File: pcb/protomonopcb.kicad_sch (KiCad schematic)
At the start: 149 parts

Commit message: Just another periodic push
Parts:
- removed LED1, LED10, LED11, LED12, LED13, LED14, LED15, LED16, LED17, LED18, LED19, LED2, LED20, LED21, LED22, LED23, LED24, LED26, LED27, LED28, LED29, LED3, LED30, LED31, LED32, LED33, LED34, LED35, LED37, LED38, LED39, LED4, LED40, LED41, LED42, LED43, LED44, LED45, LED46, LED47, LED48, LED49, LED5, LED50, LED6, LED7, LED8, LED9: SK6812MINI-E, LED_SMD:LED_SK6812MINI_PLCC4_3.5x3.5mm_P1.75mm, symbol PCM_marbastlib-various:SK6812MINI-E
- added D25, D36, D51, D52: LED, LED_THT:LED_D3.0mm, symbol Device:LED
- added R5, R6, R7, R8: 1k, Resistor_THT:R_Axial_DIN0204_L3.6mm_D1.6mm_P7.62mm_Horizontal, symbol Device:R
- A1: footprint Module:RaspberryPi_Pico_Common_Unspecified -> pico_without_keepout_area:RaspberryPi_Pico_Common_Unspecified
- CH1, CH10, CH11, CH12, CH13, CH14, CH15, CH16, CH17, CH18, CH19, CH2, CH20, CH21, CH22, CH23, CH24, CH26, CH27, CH28, CH29, CH3, CH30, CH31, CH32, CH33, CH34, CH35, CH37, CH38, CH39, CH4, CH40, CH41, CH42, CH43, CH44, CH45, CH46, CH47, CH48, CH49, CH5, CH50, CH6, CH7, CH8, CH9: footprint PCM_marbastlib-xp-gateron_lp:SW_KS33_HS_KS-2P02B01-02_HS_1u -> packed_switches_library:SW_KS33_HS_1u_18.5mm
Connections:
- net GND: now also D25.1 (K), D36.1 (K), D51.1 (K), D52.1 (K)
- net c0: now also A1.12 (GPIO9); no longer A1.14 (GPIO10), CH47.1, CH49.1
- net c1: now also A1.14 (GPIO10), CH49.1; no longer A1.15 (GPIO11), CH37.1
- net c10: now also A1.27 (GPIO21), CH50.1; no longer A1.26 (GPIO20), CH44.1
- net c11: now also A1.29 (GPIO22); no longer A1.27 (GPIO21), CH48.1, CH50.1
- net c2: now also A1.15 (GPIO11), CH37.1; no longer A1.16 (GPIO12), CH38.1
- net c3: now also A1.16 (GPIO12); no longer A1.17 (GPIO13), CH39.1
- net c4: now also A1.17 (GPIO13), CH30.1, CH38.1; no longer A1.19 (GPIO14), CH29.1, CH40.1
- net c5: now also A1.19 (GPIO14), CH29.1, CH39.1; no longer A1.20 (GPIO15), CH30.1, CH41.1
- net c6: now also A1.22 (GPIO17); no longer A1.21 (GPIO16)
- net c7: now also A1.24 (GPIO18), CH47.1; no longer A1.22 (GPIO17), CH45.1
- net c8: now also A1.25 (GPIO19); no longer A1.24 (GPIO18), CH42.1
- net c9: now also A1.26 (GPIO20), CH44.1; no longer A1.25 (GPIO19), CH43.1
- net r0: now also D1.2 (A), D10.2 (A), D12.2 (A), D3.2 (A), D4.2 (A), D49.2 (A), D5.2 (A), D50.2 (A), D6.2 (A), D7.2 (A), D8.2 (A), D9.2 (A); no longer D37.2 (A), D38.2 (A), D39.2 (A), D40.2 (A), D41.2 (A), D42.2 (A), D43.2 (A), D44.2 (A), D45.2 (A), D46.2 (A), D47.2 (A), D48.2 (A)
- net r1: now also D11.2 (A), D15.2 (A), D16.2 (A), D17.2 (A), D18.2 (A), D19.2 (A), D2.2 (A), D20.2 (A), D21.2 (A), D22.2 (A), D42.2 (A), D48.2 (A); no longer D26.2 (A), D27.2 (A), D28.2 (A), D29.2 (A), D30.2 (A), D31.2 (A), D32.2 (A), D33.2 (A), D34.2 (A), D35.2 (A)
- net r2: now also D27.2 (A), D28.2 (A), D29.2 (A), D30.2 (A), D31.2 (A), D32.2 (A), D33.2 (A), D34.2 (A), D41.2 (A), D43.2 (A); no longer D1.2 (A), D12.2 (A), D15.2 (A), D16.2 (A), D17.2 (A), D18.2 (A), D19.2 (A), D20.2 (A), D21.2 (A), D22.2 (A)
- net r3: now also D26.2 (A), D35.2 (A), D37.2 (A), D38.2 (A), D39.2 (A), D40.2 (A), D44.2 (A), D45.2 (A), D46.2 (A), D47.2 (A); no longer D10.2 (A), D11.2 (A), D2.2 (A), D3.2 (A), D4.2 (A), D49.2 (A), D5.2 (A), D50.2 (A), D6.2 (A), D7.2 (A), D8.2 (A), D9.2 (A)
- net at R1.1: now also A1.7 (GPIO5); no longer A1.9 (GPIO6)
- net at R2.1: now also A1.9 (GPIO6); no longer A1.10 (GPIO7)
- net at R3.1: now also A1.10 (GPIO7); no longer A1.11 (GPIO8)
- net at R4.1: now also A1.11 (GPIO8); no longer A1.12 (GPIO9)
- net LED_1: now reaches A1.2 (GPIO1)
- net LED_1: now also R6.1
- net LED_2: now reaches A1.4 (GPIO2)
- net LED_2: now also R7.1
- net LED_3: now reaches A1.5 (GPIO3)
- net LED_3: now also R8.1
- net LED_in renamed LED_0
- net LED_0: now also R5.1
- new net: D52.2 (A), R8.2
- new net: D51.2 (A), R7.2
- new net: D25.2 (A), R5.2
- new net: D36.2 (A), R6.2
- new net ci: A1.20 (GPIO15), CH40.1, CH41.1, CH42.1
- new net cii: A1.21 (GPIO16), CH43.1, CH45.1, CH48.1
- no-connect marks 16 -> 10
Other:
- moved on the sheet: A1, CH1, CH10, CH11, CH12, CH13, CH14, CH15, CH16, CH17, CH18, CH19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

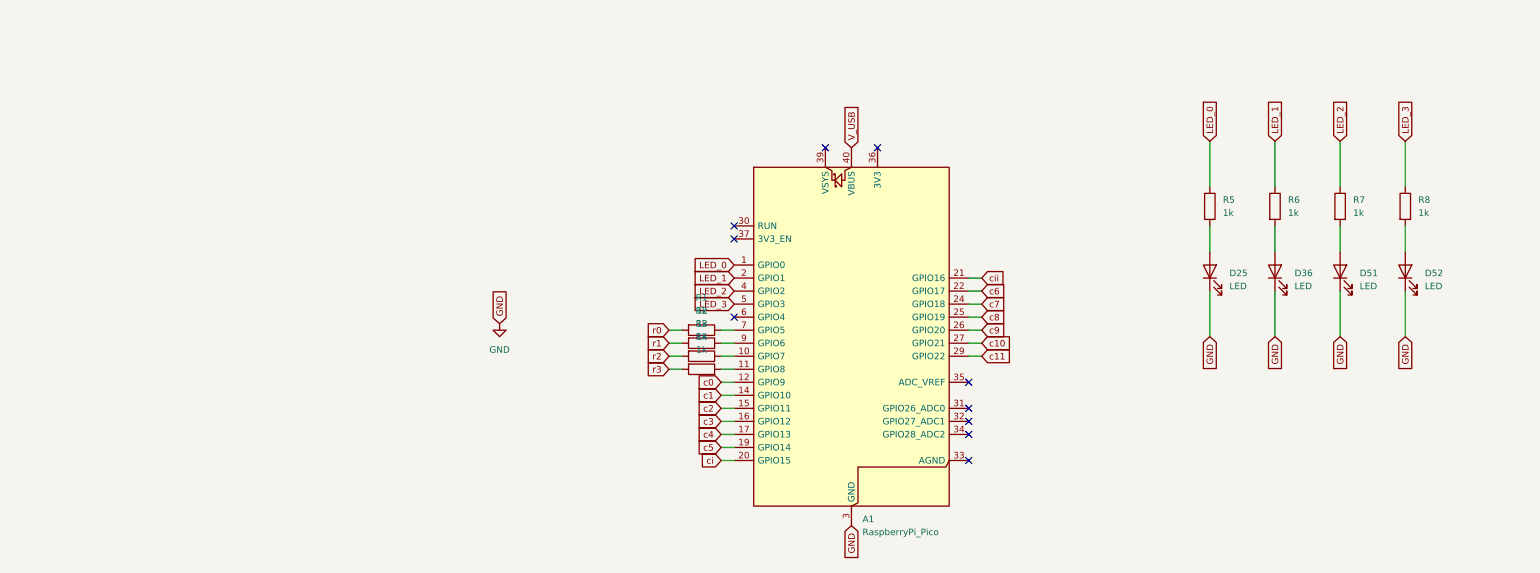
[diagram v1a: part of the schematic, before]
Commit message: Bottom PCB completed
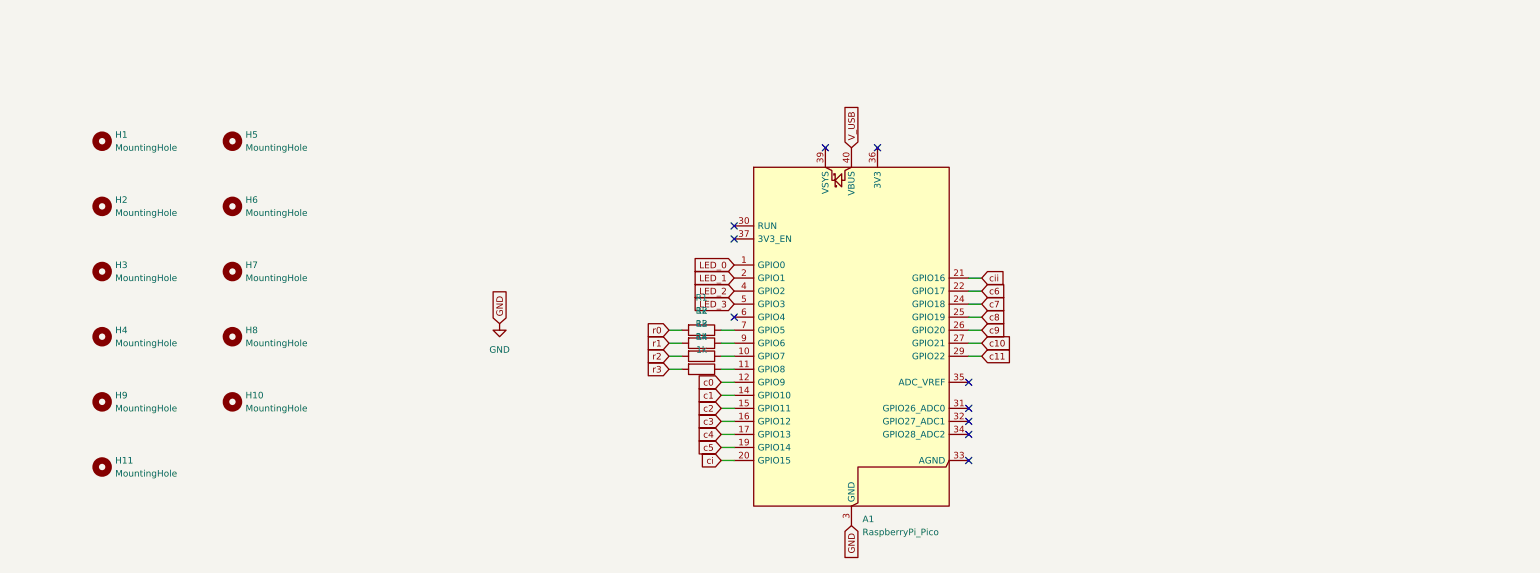
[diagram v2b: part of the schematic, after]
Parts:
- removed D25, D36, D51, D52: LED, LED_THT:LED_D3.0mm, symbol Device:LED
- removed R5, R6, R7, R8: 1k, Resistor_THT:R_Axial_DIN0204_L3.6mm_D1.6mm_P7.62mm_Horizontal, symbol Device:R
- added H1, H10, H11, H2, H3, H4, H5, H6, H7, H8, H9: MountingHole, MountingHole:MountingHole_3.2mm_M3_Pad_Via, symbol Mechanical:MountingHole
